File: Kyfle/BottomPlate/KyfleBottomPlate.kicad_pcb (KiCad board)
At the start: 2 copper layers, 164 x 146.3 mm, 50 parts, among them SW2 15°, SW2 19°, SW2 25°, SW2 30°, SW2 35°, SW2 40°, SW2 45°, SW2 KEY_SWITCH, SW2 PRO MICRO

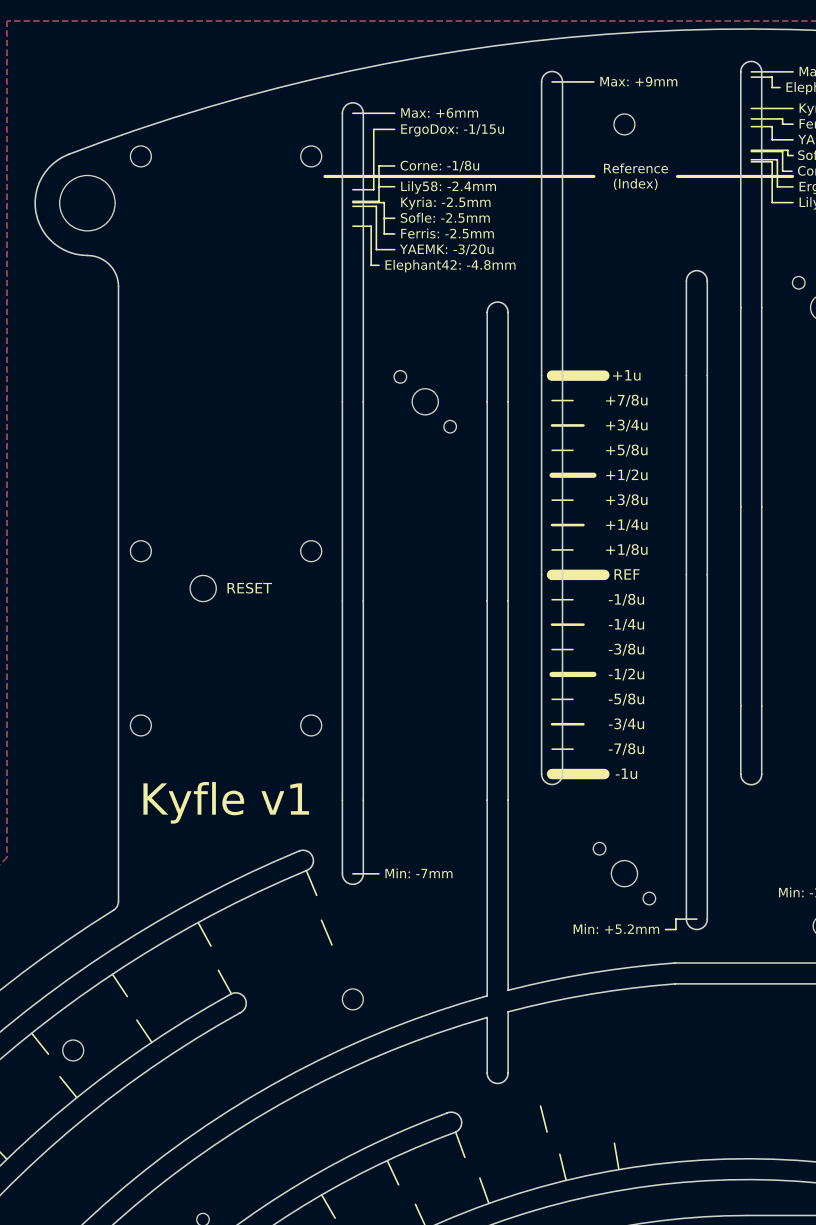
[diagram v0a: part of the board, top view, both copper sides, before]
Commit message: It is never done. Adding plethora of plate variants.
- Variant of the default top plate with less routing involved
- Variant of a top plate allowing to slide the switches around
- Variant of that last top plate with less routing involved

Also moving few minor things here and there.
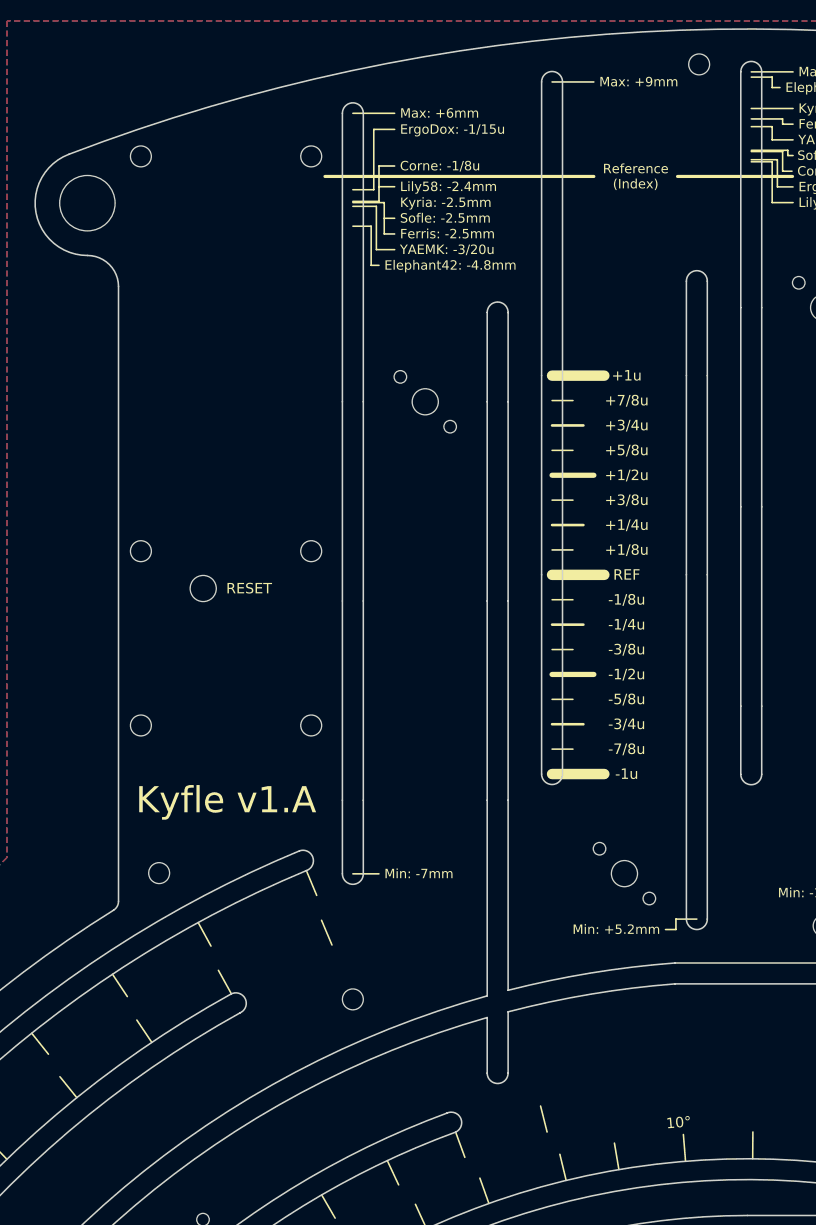
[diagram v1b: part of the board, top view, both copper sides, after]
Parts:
- added SW2: 5°, Kyfle Footprints:CherryMX_Kyfle_v1_BottomPlate_1u_No_Rail_Angle_Silk, F.Cu at (154.6, 118.4)
- added SW2: 10°, Kyfle Footprints:CherryMX_Kyfle_v1_BottomPlate_1u_No_Rail_Angle_Silk, F.Cu at (147.5, 119.4)
- moved TH7 18.8 mm to (105.5, 99.0)
- moved TH3 9.16 mm to (157.1, 21.7), turned to 90 degrees
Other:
- board text added: "Kyfle v1.A"
- board text removed: "Kyfle v1"
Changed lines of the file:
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@@
-(kicad_pcb (version 20171130) (host pcbnew 5.1.11-e4df9d881f~92~ubuntu20.04.1)
+(kicad_pcb (version 20171130) (host pcbnew 5.1.10-88a1d61d58~88~ubuntu18.04.1)
   (general
     (thickness 1.6)
@@
     (tracks 0)
     (zones 0)
-    (modules 50)
+    (modules 52)
     (nets 1)
   )
@@
     (34 B.Paste user hide)
     (35 F.Paste user hide)
-    (36 B.SilkS user)
+    (36 B.SilkS user hide)
     (37 F.SilkS user)
     (38 B.Mask user hide)
@@
     (pad_to_mask_clearance 0)
     (aux_axis_origin 0 0)
-    (grid_origin 188.1 98.55)
+    (grid_origin 169.05 92.55)
     (visible_elements 7FFEFF7F)
     (pcbplotparams
@@
     (uvia_drill 0.1)
   )
+  (module "Kyfle Footprints:CherryMX_Kyfle_v1_BottomPlate_1u_No_Rail_Angle_Silk" (layer F.Cu)
+    (at 154.624941 118.435141 5)
+    (fp_text reference SW2 (at 0 3 5) (layer F.Fab) hide
+      (effects (font (size 1 1) (thickness 0.15)))
+    )
+    (fp_text value 5° (at 0 -3 5) (layer F.Fab) hide
+      (effects (font (size 1 1) (thickness 0.15)))
+    )
+    (fp_line (start 6.92375 8.525) (end 7.165785 5.964539) (layer F.SilkS) (width 0.153))
+    (fp_circle (center -6.92375 9.525) (end -5.92375 9.525) (layer Eco2.User) (width 0.12))
+    (fp_circle (center 6.92375 -9.525) (end 7.92375 -9.525) (layer Eco2.User) (width 0.12))
+    (fp_circle (center 6.92375 9.525) (end 7.92375 9.525) (layer Eco2.User) (width 0.12))
+    (fp_circle (center -6.92375 -9.525) (end -5.92375 -9.525) (layer Eco2.User) (width 0.12))
+    (fp_line (start 9.025 -9.025) (end 9.025 9.025) (layer F.CrtYd) (width 0.12))
+    (fp_line (start -9.025 9.025) (end -9.025 -9.025) (layer F.CrtYd) (width 0.12))
+    (fp_line (start 9.025 9.025) (end -9.025 9.025) (layer F.CrtYd) (width 0.12))
+    (fp_circle (center 6.92375 9.525) (end 7.92375 9.525) (layer F.CrtYd) (width 0.12))
+    (fp_circle (center -6.92375 -9.525) (end -5.92375 -9.525) (layer F.CrtYd) (width 0.12))
+    (fp_circle (center 6.92375 -9.525) (end 7.92375 -9.525) (layer F.CrtYd) (width 0.12))
+    (fp_line (start -9.025 -9.025) (end 9.025 -9.025) (layer F.CrtYd) (width 0.12))
+    (fp_circle (center -6.92375 9.525) (end -5.92375 9.525) (layer F.CrtYd) (width 0.12))
+    (fp_line (start 9.525 -9.525) (end -9.525 -9.525) (layer F.Fab) (width 0.15))
+    (fp_line (start -9.525 -9.525) (end -9.525 9.525) (layer F.Fab) (width 0.15))
+    (fp_line (start -9.525 9.525) (end 9.525 9.525) (layer F.Fab) (width 0.15))
+    (fp_line (start 9.525 9.525) (end 9.525 -9.525) (layer F.Fab) (width 0.15))
+    (fp_line (start 6.92375 8.525) (end 7.165785 5.964539) (layer B.SilkS) (width 0.153))
+    (fp_text user %V (at 6.92375 4.7625 359.9) (layer B.SilkS)
+      (effects (font (size 1 1) (thickness 0.15)) (justify mirror))
+    )
+    (fp_text user %V (at 6.92375 4.7625 359.9) (layer F.SilkS)
+      (effects (font (size 1 1) (thickness 0.15)))
+    )
+    (model ${ACHERONLIB}/3d_models/mx_switch.step
+      (offset (xyz -7.35 -7.3 0))
+      (scale (xyz 1 1 1))
+      (rotate (xyz -90 0 0))
+    )
+  )
+  (module "Kyfle Footprints:CherryMX_Kyfle_v1_BottomPlate_1u_No_Rail_Angle_Silk" (layer F.Cu)
+    (at 147.543805 119.36739 10)
+    (fp_text reference SW2 (at 0 3 10) (layer F.Fab) hide
+      (effects (font (size 1 1) (thickness 0.15)))
+    )
+    (fp_text value 10° (at 0 -3 10) (layer F.Fab) hide
+      (effects (font (size 1 1) (thickness 0.15)))
+    )
+    (fp_line (start 6.92375 8.525) (end 7.165785 5.964539) (layer B.SilkS) (width 0.153))
+    (fp_line (start 9.525 9.525) (end 9.525 -9.525) (layer F.Fab) (width 0.15))
+    (fp_line (start -9.525 9.525) (end 9.525 9.525) (layer F.Fab) (width 0.15))
+    (fp_line (start -9.525 -9.525) (end -9.525 9.525) (layer F.Fab) (width 0.15))
+    (fp_line (start 9.525 -9.525) (end -9.525 -9.525) (layer F.Fab) (width 0.15))
+    (fp_circle (center -6.92375 9.525) (end -5.92375 9.525) (layer F.CrtYd) (width 0.12))
+    (fp_line (start -9.025 -9.025) (end 9.025 -9.025) (layer F.CrtYd) (width 0.12))
+    (fp_circle (center 6.92375 -9.525) (end 7.92375 -9.525) (layer F.CrtYd) (width 0.12))
+    (fp_circle (center -6.92375 -9.525) (end -5.92375 -9.525) (layer F.CrtYd) (width 0.12))
+    (fp_circle (center 6.92375 9.525) (end 7.92375 9.525) (layer F.CrtYd) (width 0.12))
+    (fp_line (start 9.025 9.025) (end -9.025 9.025) (layer F.CrtYd) (width 0.12))
+    (fp_line (start -9.025 9.025) (end -9.025 -9.025) (layer F.CrtYd) (width 0.12))
+    (fp_line (start 9.025 -9.025) (end 9.025 9.025) (layer F.CrtYd) (width 0.12))
+    (fp_circle (center -6.92375 -9.525) (end -5.92375 -9.525) (layer Eco2.User) (width 0.12))
+    (fp_circle (center 6.92375 9.525) (end 7.92375 9.525) (layer Eco2.User) (width 0.12))
+    (fp_circle (center 6.92375 -9.525) (end 7.92375 -9.525) (layer Eco2.User) (width 0.12))
+    (fp_circle (center -6.92375 9.525) (end -5.92375 9.525) (layer Eco2.User) (width 0.12))
+    (fp_line (start 6.92375 8.525) (end 7.165785 5.964539) (layer F.SilkS) (width 0.153))
+    (fp_text user %V (at 6.92375 4.7625 184.9) (layer F.SilkS)
+      (effects (font (size 1 1) (thickness 0.15)))
+    )
+    (fp_text user %V (at 6.92375 4.7625 184.9) (layer B.SilkS)
+      (effects (font (size 1 1) (thickness 0.15)) (justify mirror))
+    )
+    (model ${ACHERONLIB}/3d_models/mx_switch.step
+      (offset (xyz -7.35 -7.3 0))
+      (scale (xyz 1 1 1))
+      (rotate (xyz -90 0 0))
+    )
+  )
   (module "Kyfle Footprints:Arduino_ProMicro_Kyfle_v1_BottomPlate" (layer F.Cu)
     (at 111.9 58.6875)
@@
     (fp_text value "PRO MICRO" (at 0 -4) (layer F.Fab) hide
       (effects (font (size 1 1) (thickness 0.15)))
-    )
-    (fp_text user RESET (at 0 13.096875) (layer B.SilkS)
-      (effects (font (size 1 1) (thickness 0.15)) (justify right mirror))
-    )
-    (fp_text user RESET (at 0 13.096875) (layer F.SilkS)
-      (effects (font (size 1 1) (thickness 0.15)) (justify left))
     )
     (fp_circle (center 8.14375 26.19375) (end 10.14375 26.19375) (layer F.CrtYd) (width 0.05))
@@
     (fp_circle (center 3.81 7.94) (end 4.21 7.94) (layer F.CrtYd) (width 0.12))
     (fp_circle (center -3.81 7.94) (end -3.41 7.94) (layer F.CrtYd) (width 0.12))
+    (fp_text user RESET (at 0 13.096875) (layer B.SilkS)
+      (effects (font (size 1 1) (thickness 0.15)) (justify right mirror))
+    )
+    (fp_text user RESET (at 0 13.096875) (layer F.SilkS)
+      (effects (font (size 1 1) (thickness 0.15)) (justify left))
+    )
     (pad "" np_thru_hole circle (at -8.14375 9.525) (size 2 2) (drill 2) (layers *.Cu *.Mask)
       (clearance 1.1))
@@
   )
   (module "Kyfle Footprints:M2_with_washer" (layer F.Cu)
-    (at 97.280371 115.961615 90)
+    (at 105.5 99 90)
     (descr "Mounting Hole 2.2mm, no annular, M2, ISO14580")
     (tags "mounting hole 2.2mm no annular m2 iso14580")
@@
   )
   (module "Kyfle Footprints:M2_with_washer" (layer F.Cu)
-    (at 150 27.4)
+    (at 157.14375 21.659375 90)
     (descr "Mounting Hole 2.2mm, no annular, M2, ISO14580")
     (tags "mounting hole 2.2mm no annular m2 iso14580")
     (attr virtual)
-    (fp_text reference TH3 (at 0 -2.9) (layer B.Fab) hide
-      (effects (font (size 1 1) (thickness 0.15)))
-    )
-    (fp_text value HOLE (at 0 2.9) (layer F.Fab)
+    (fp_text reference TH3 (at 0 -2.9 90) (layer B.Fab) hide
+      (effects (font (size 1 1) (thickness 0.15)))
+    )
+    (fp_text value HOLE (at 0 2.9 90) (layer F.Fab)
       (effects (font (size 1 1) (thickness 0.15)))
     )
     (fp_circle (center 0 0) (end 2 0) (layer F.CrtYd) (width 0.05))
-    (fp_text user %R (at 0.3 0) (layer F.Fab)
-      (effects (font (size 1 1) (thickness 0.15)))
-    )
-    (pad "" np_thru_hole circle (at 0 0) (size 2 2) (drill 2) (layers *.Cu *.Mask)
+    (fp_text user %R (at 0.3 0 90) (layer F.Fab)
+      (effects (font (size 1 1) (thickness 0.15)))
+    )
+    (pad "" np_thru_hole circle (at 0 0 90) (size 2 2) (drill 2) (layers *.Cu *.Mask)
       (clearance 1.1))
   )
@@
     (effects (font (size 0.9 0.9) (thickness 0.15)) (justify left))
   )
-  (gr_text "Kyfle v1" (at 111.9 92.025) (layer B.SilkS)
-    (effects (font (size 3 3) (thickness 0.6)) (justify mirror))
+  (gr_text "Kyfle v1.A" (at 111.9 92.025) (layer B.SilkS)
+    (effects (font (size 2.5 2.5) (thickness 0.5)) (justify mirror))
   )
   (gr_text "YAEMK: -5/7u" (at 202.72625 45.875) (layer B.SilkS)
@@
   (gr_arc (start 100.614896 101.696643) (end 101.143092 102.545766) (angle -58.1) (layer Edge.Cuts) (width 0.15))
   (gr_line (start 101.614896 42.905771) (end 101.614896 101.696929) (layer Edge.Cuts) (width 0.15))
-  (gr_text "Kyfle v1" (at 111.9 92.025) (layer F.SilkS)
-    (effects (font (size 3 3) (thickness 0.6)))
+  (gr_text "Kyfle v1.A" (at 111.9 92.025) (layer F.SilkS)
+    (effects (font (size 2.5 2.5) (thickness 0.5)))
   )
   (gr_line (start 188.75 122.2) (end 180.29 102.55) (layer B.Fab) (width 0.15))

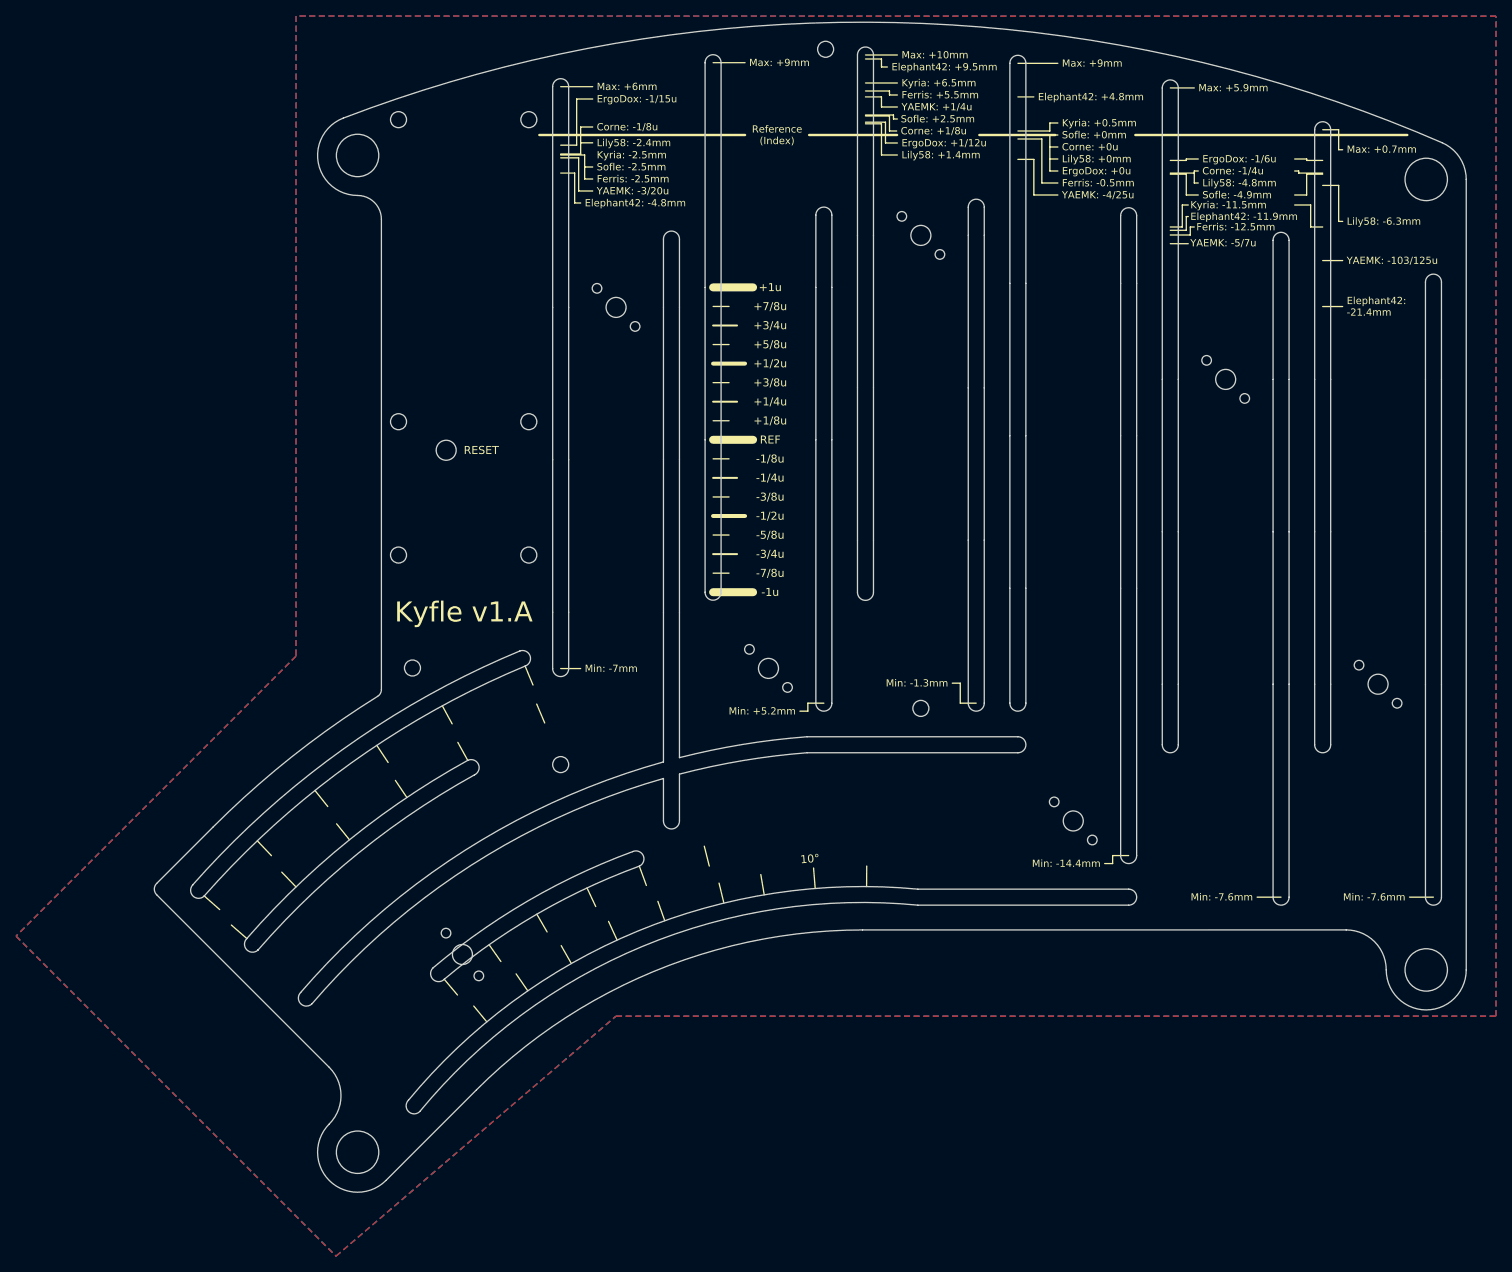
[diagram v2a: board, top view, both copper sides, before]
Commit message: Plates: Received M2 and M5 hardware. It's bigger than specified...
- M5 screw head is ~9.5 instead of 8.7. Was colliding in the top left 
corner with M2 screw for pro micro board. So I shifted up pro micro 
board 0.3mm.
- M2 screw head is also larger than expected (3.8 instead of 3.2). But 
it is mostly fine as I was designing with 4-4.2mm clearance. Only 
exception was for screws supporting the middle bottom section of top 
plate with rails. Here it was colliding with switch housing. So, only 
solution is to use so called reduced slotted screws (DIN 920) as they 
have 2.8mm diameter head.
- Also added JLCPCB silk reference
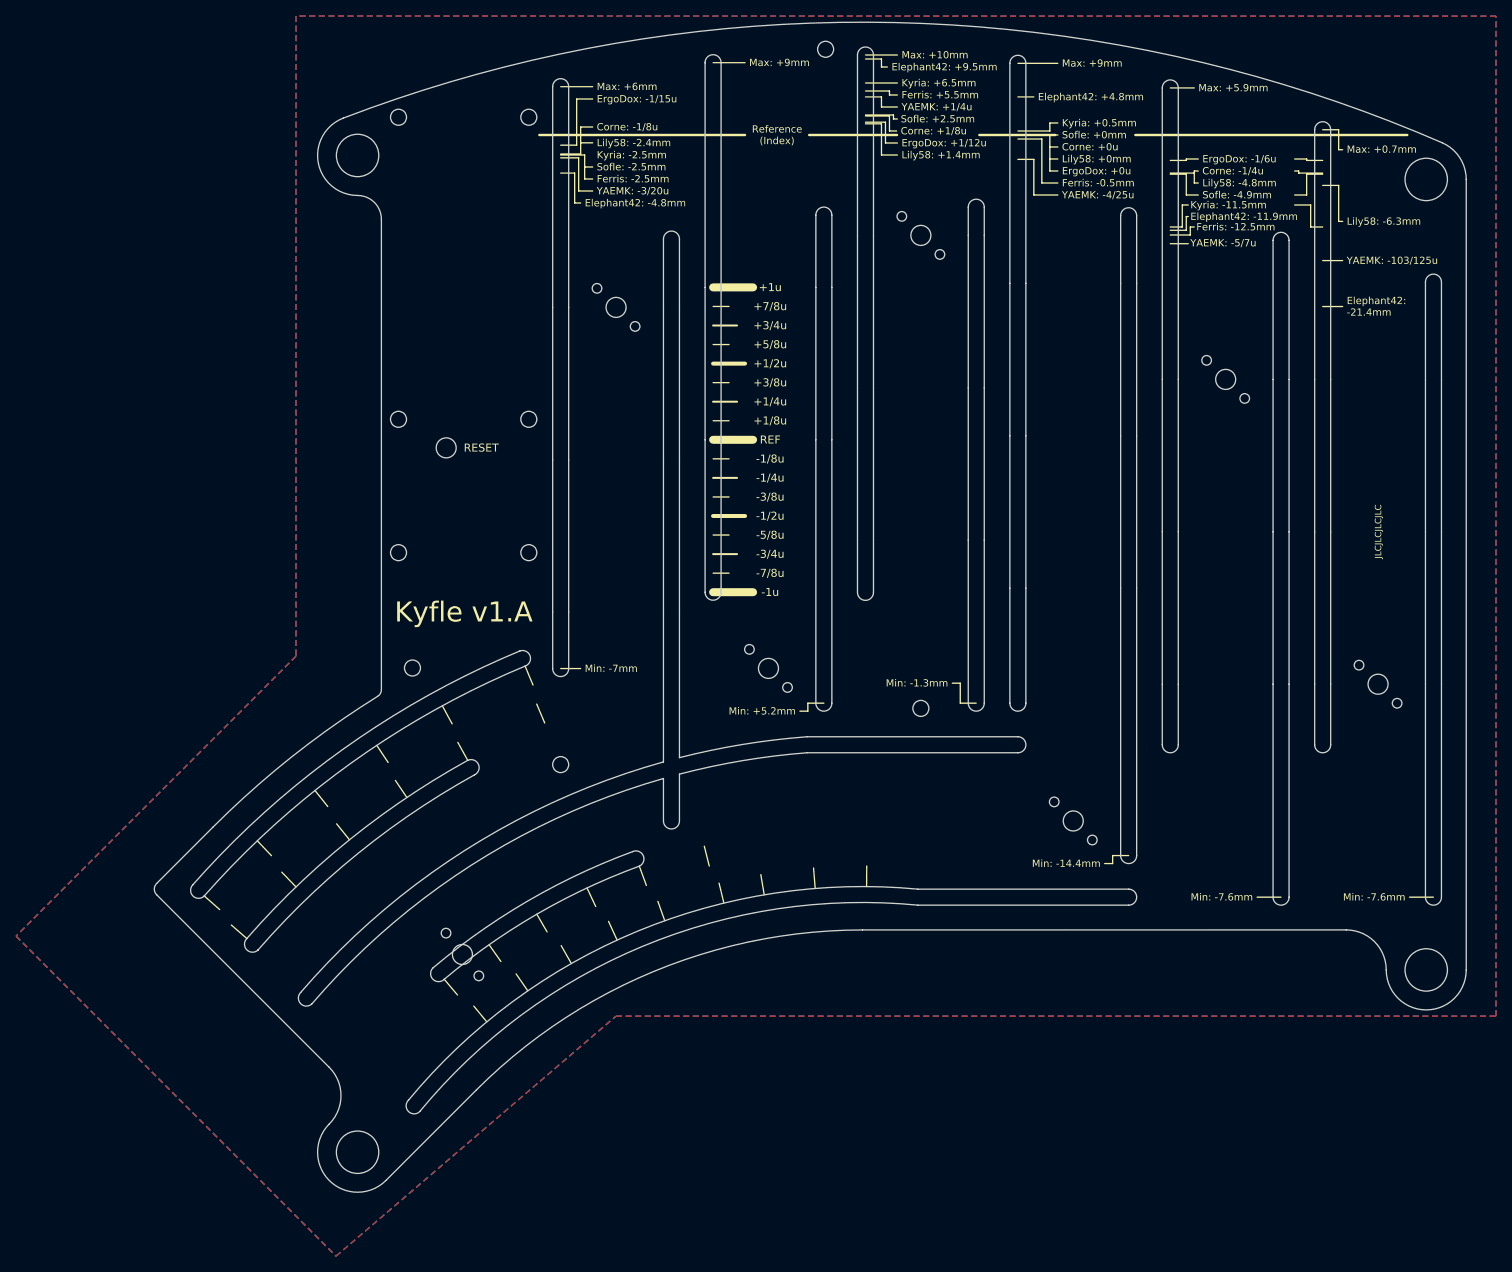
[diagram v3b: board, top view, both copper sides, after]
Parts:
- added JLCJLCJLCJLC: JLCBCB_OrderNumber, Kyfle Footprints:JLCBCB_OrderNumber, F.Cu at (226.2, 82.0)
- moved SW2 0.30 mm to (111.9, 58.4)

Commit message: Adding mouse bites to top plate (rail-less only for now)
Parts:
- added REF**: RollerEncoder_Panasonic_EVQWGD001, Kyfle Footprints:RollerEncoder_TopPlate, F.Cu at (180.8, 118.1)
